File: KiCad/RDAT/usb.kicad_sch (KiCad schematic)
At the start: 5 parts, among them J5 USB_A_Stacked, U9 ULC0524P

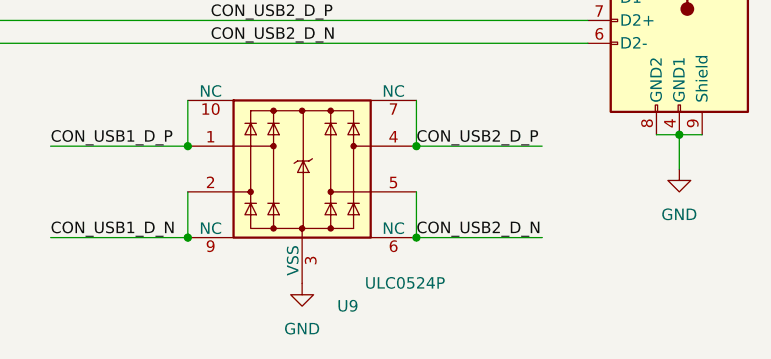
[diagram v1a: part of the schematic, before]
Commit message: Added Libs and DOCS
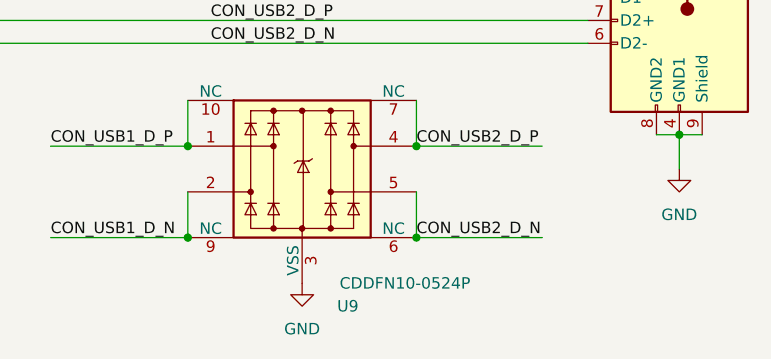
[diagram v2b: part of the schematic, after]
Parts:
- J5: footprint A_HDJ_Library:USB_A_CUI_UJ2-ADH-TH_Horizontal_Stacked -> footprints:CONN8_MUSBC_1211x569_AMP
- U9: value ULC0524P -> CDDFN10-0524P; JLCPCB_LINK (none) -> https://jlcpcb.com/partdetail/Bourns-CDDFN100524P/C911379
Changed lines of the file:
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@@
 			)
 		)
-		(property "Value" "ULC0524P"
+		(property "Value" "CDDFN10-0524P"
 			(at 133.35 82.55 0)
 			(effects
@@
 			)
 		)
-		(property "Datasheet" "https://www.diodes.com/assets/Datasheets/D3V3XA4B10LP.pdf"
+		(property "Datasheet" "https://wmsc.lcsc.com/wmsc/upload/file/pdf/v2/lcsc/2103161034_BOURNS-CDDFN10-0524P_C911379.pdf"
 			(at 121.92 69.85 0)
 			(effects
@@
 			)
 		)
-		(property "JLCPCB_LINK" ""
-			(at 121.92 69.85 0)
-			(effects
-				(font
-					(size 1.27 1.27)
-				)
+		(property "JLCPCB_LINK" "https://jlcpcb.com/partdetail/Bourns-CDDFN100524P/C911379"
+			(at 121.92 69.85 0)
+			(effects
+				(font
+					(size 1.27 1.27)
+				)
+				(hide yes)
 			)
 		)
@@
 			)
 		)
-		(property "Footprint" "A_HDJ_Library:USB_A_CUI_UJ2-ADH-TH_Horizontal_Stacked"
+		(property "Footprint" "footprints:CONN8_MUSBC_1211x569_AMP"
 			(at 160.02 64.77 0)
 			(effects

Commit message: Sourced and documented all parts
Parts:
- C51: JLCPCB_LINK (none) -> https://jlcpcb.com/partdetail/4414076-GRM158R61A226ME15D/C3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
- F2, F3: JLCPCB_LINK (none) -> https://jlcpcb.com/partdetail/Littelfuse-0805L100WR/C80270
- J5: JLCPCB_LINK (none) -> https://www.digikey.com/en/products/detail/amphenol-cs-comm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
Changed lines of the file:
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@@
 			)
 		)
-		(property "Datasheet" "~"
+		(property "Datasheet" "https://www.lcsc.com/datasheet/lcsc_datasheet_2304140030_Littelfuse-0805L100WR_C80270.pdf"
 			(at 144.78 40.64 0)
 			(effects
@@
 			)
 		)
-		(property "JLCPCB_LINK" ""
+		(property "JLCPCB_LINK" "https://jlcpcb.com/partdetail/Littelfuse-0805L100WR/C80270"
 			(at 144.78 40.64 0)
 			(effects
@@
 					(size 1.27 1.27)
 				)
+				(hide yes)
 			)
 		)
@@
 			)
 		)
-		(property "Datasheet" "~"
+		(property "Datasheet" "https://www.lcsc.com/datasheet/lcsc_datasheet_2304140030_Littelfuse-0805L100WR_C80270.pdf"
 			(at 144.78 43.18 0)
 			(effects
@@
 			)
 		)
-		(property "JLCPCB_LINK" ""
+		(property "JLCPCB_LINK" "https://jlcpcb.com/partdetail/Littelfuse-0805L100WR/C80270"
 			(at 144.78 43.18 0)
 			(effects
@@
 					(size 1.27 1.27)
 				)
+				(hide yes)
 			)
 		)
@@
 			)
 		)
-		(property "Datasheet" "~"
+		(property "Datasheet" "https://jlcpcb.com/api/file/downloadByFileSystemAccessId/8558969697804193792"
 			(at 128.27 40.64 0)
 			(effects
@@
 			)
 		)
-		(property "JLCPCB_LINK" ""
+		(property "JLCPCB_LINK" "https://jlcpcb.com/partdetail/4414076-GRM158R61A226ME15D/C3845593"
 			(at 128.27 40.64 0)
 			(effects
@@
 					(size 1.27 1.27)
 				)
+				(hide yes)
 			)
 		)
@@
 			)
 		)
-		(property "Datasheet" "~"
+		(property "Datasheet" "https://www.amphenol-icc.com/media/wysiwyg/files/drawing/musbc111xx.pdf"
 			(at 158.75 49.53 0)
 			(effects
@@
 			)
 		)
-		(property "JLCPCB_LINK" ""
+		(property "JLCPCB_LINK" "https://www.digikey.com/en/products/detail/amphenol-cs-commercial-products/MUSBC111M0/4889538"
 			(at 163.83 50.8 0)
 			(effects
@@
 					(size 1.27 1.27)
 				)
-			)
-		)
+				(hide yes)
+			)
+		)

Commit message: Push before Board Layout
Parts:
- C51: footprint A_HDJ_Library:C_0603_1608Metric -> Capacitor_SMD:C_0402_1005Metric
- F2, F3: footprint A_HDJ_Library:Fuse_0805_2012Metric -> Fuse:Fuse_0805_2012Metric
- U9: footprint A_HDJ_Library:Diodes_UDFN-10_1.0x2.5mm_P0.5mm -> Package_DFN_QFN:Diodes_UDFN-10_1.0x2.5mm_P0.5mm
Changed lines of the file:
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@@
 			)
 		)
-		(property "Footprint" "A_HDJ_Library:Fuse_0805_2012Metric"
+		(property "Footprint" "Fuse:Fuse_0805_2012Metric"
 			(at 144.78 42.418 90)
 			(effects
@@
 			)
 		)
-		(property "Footprint" "A_HDJ_Library:Fuse_0805_2012Metric"
+		(property "Footprint" "Fuse:Fuse_0805_2012Metric"
 			(at 144.78 44.958 90)
 			(effects
@@
 			)
 		)
-		(property "Footprint" "A_HDJ_Library:Diodes_UDFN-10_1.0x2.5mm_P0.5mm"
+		(property "Footprint" "Package_DFN_QFN:Diodes_UDFN-10_1.0x2.5mm_P0.5mm"
 			(at 97.79 80.01 0)
 			(effects
@@
 			)
 		)
-		(property "Footprint" "A_HDJ_Library:C_0603_1608Metric"
+		(property "Footprint" "Capacitor_SMD:C_0402_1005Metric"
 			(at 132.08 39.6748 0)
 			(effects

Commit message: End Of day commit
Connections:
- net GND: no longer J5.9 (Shield)
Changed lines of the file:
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@@
-	(wire
-		(pts
-			(xy 163.83 66.04) (xy 166.37 66.04)
-		)
-		(stroke
-			(width 0)
-			(type default)
-		)
-	)
 	(wire
 		(pts
@@
 		(pin "2"
 		)
-		(pin "9"
-		)
 		(instances

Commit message: Most of the way thru routing
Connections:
- net USB_2_P3+: now also U9.5, U9.6 (NC); no longer U9.4, U9.7 (NC)
- net USB_2_P3-: now also U9.4, U9.7 (NC); no longer U9.5, U9.6 (NC)
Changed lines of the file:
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@@
 	)
 	(label "CON_USB2_D_N"
+		(at 135.89 67.31 0)
+		(effects
+			(font
+				(size 1.27 1.27)
+			)
+			(justify left bottom)
+		)
+	)
+	(label "CON_USB2_D_P"
 		(at 134.62 77.47 0)
 		(effects
@@
 		(effects
 			(font
-				(size 1.27 1.27)
-			)
-			(justify left bottom)
-		)
-	)
-	(label "CON_USB2_D_P"
-		(at 134.62 67.31 0)
-		(effects
-			(font

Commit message: 2x checing of bom on JLCPCB
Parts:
- C51: value 22uF/10V -> 22uF
- U9: JLCPCB_PART_NUMBER (none) -> C911379
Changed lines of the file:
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@@
+			)
+		)
+		(property "JLCPCB_PART_NUMBER" ""
+			(at 144.78 40.64 0)
+			(effects
+				(font
+					(size 1.27 1.27)
+				)
 			)
 		)
@@
 			)
 		)
+		(property "JLCPCB_PART_NUMBER" ""
+			(at 144.78 43.18 0)
+			(effects
+				(font
+					(size 1.27 1.27)
+				)
+			)
+		)
 		(pin "1"
 		)
@@
 				)
 				(hide yes)
+			)
+		)
+		(property "JLCPCB_PART_NUMBER" "C911379"
+			(at 121.92 69.85 0)
+			(effects
+				(font
+					(size 1.27 1.27)
+				)
 			)
 		)
@@
 			)
 		)
-		(property "Value" "22uF/10V"
+		(property "Value" "22uF"
 			(at 124.46 36.83 90)
 			(effects
@@
 				)
 				(hide yes)
+			)
+		)
+		(property "JLCPCB_PART_NUMBER" ""
+			(at 128.27 40.64 0)
+			(effects
+				(font
+					(size 1.27 1.27)
+				)
 			)
 		)
@@
 			)
 		)
+		(property "JLCPCB_PART_NUMBER" ""
+			(at 163.83 50.8 0)
+			(effects
+				(font
+					(size 1.27 1.27)
+				)
+			)
+		)
